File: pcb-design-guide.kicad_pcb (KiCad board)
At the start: 2 copper layers, 24 parts, among them SW1 SW_Push, U1 ATmega32U4-AU, Y1 16MHz

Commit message: PCB design complete
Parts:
- moved C2 24.5 mm to (192.3, 82.0), turned to 0 degrees
- moved C6 23.9 mm to (183.3, 59.6), turned to 90 degrees
- moved C3 13.3 mm to (182.8, 82.2)
- moved C7 12.8 mm to (175.9, 70.4), turned to 180 degrees
- moved C1 8.74 mm to (197.1, 67.2)
- moved C5 8.64 mm to (191.9, 59.4)
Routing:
- net COL1: track 0.00 -> 72.6 mm, vias 0 -> 1
- net +5V: track 41.7 -> 103.2 mm, vias 0 -> 6
- net COL0: track 0.00 -> 40.3 mm, vias 0 -> 1
- net Net-(R3-Pad2): track 14.2 -> 47.7 mm, vias 0 -> 2
- net Net-(C5-Pad1): track 24.5 -> 9.07 mm
- net GND: track 146.5 -> 153.7 mm
- net Net-(C7-Pad1): track 0.00 -> 5.24 mm
- net Net-(C6-Pad1): track 9.43 -> 11.0 mm

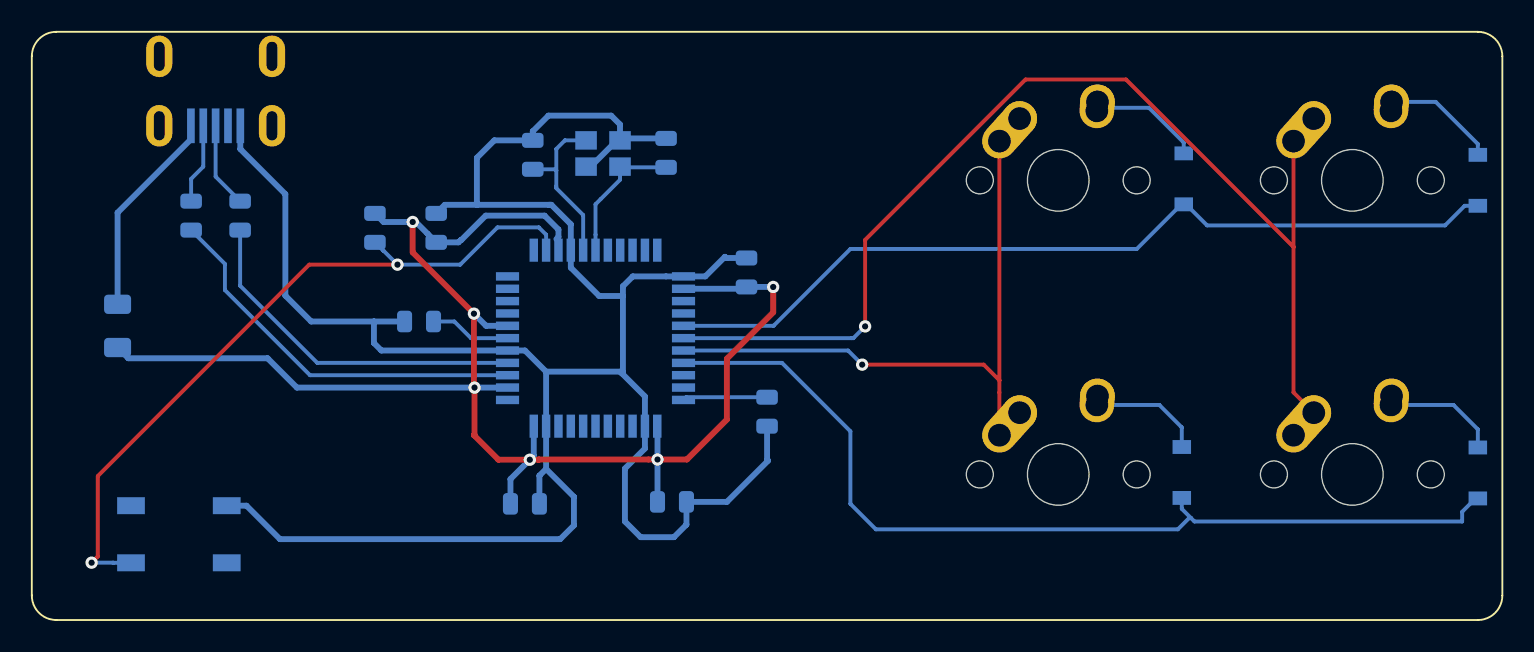
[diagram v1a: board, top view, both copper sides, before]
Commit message: Added ground fills
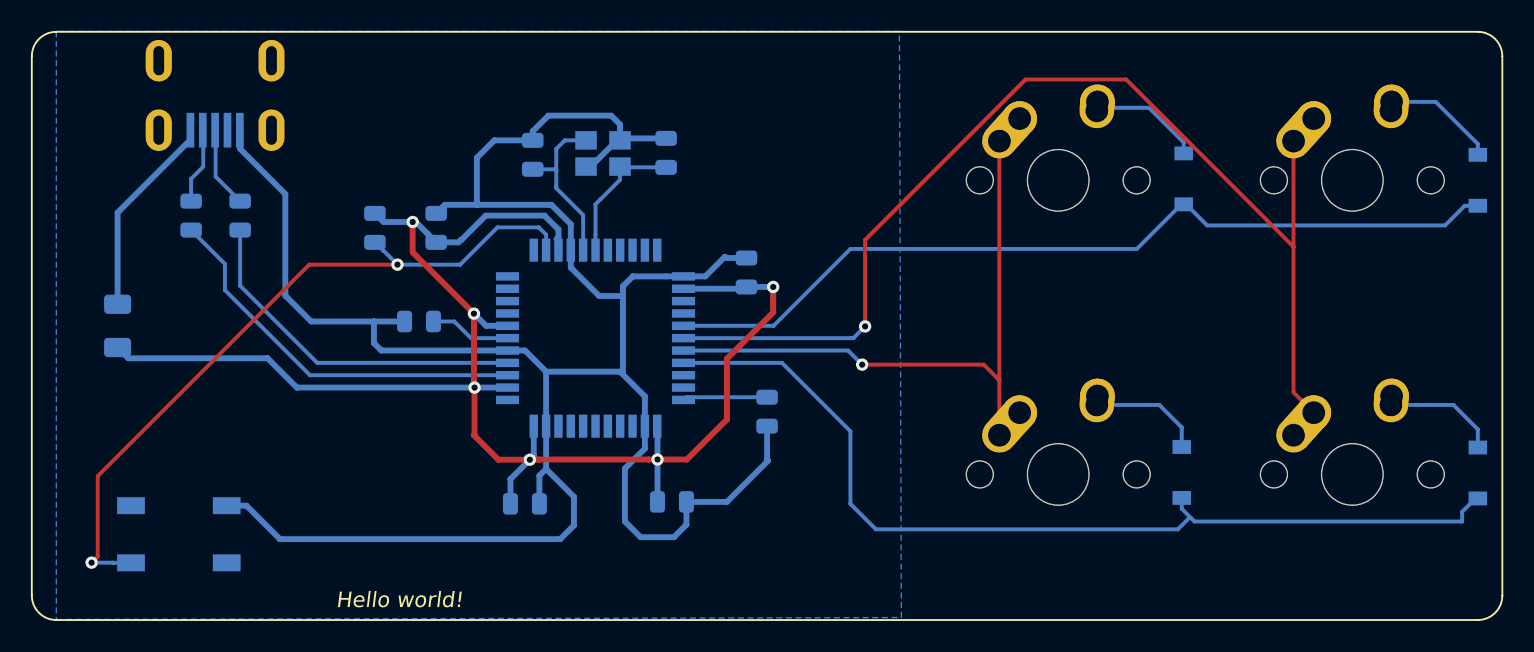
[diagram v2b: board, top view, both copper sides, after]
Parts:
- moved USB1 0.29 mm to (162.7, 53.5)
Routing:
- added copper zone on B.Cu, net GND
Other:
- board text added: "Hello world!"
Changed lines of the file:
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@@
   (general
     (thickness 1.6)
-    (drawings 8)
+    (drawings 9)
     (tracks 240)
     (zones 0)
@@
   )
   (module random-keyboard-parts:Molex-0548190589 (layer B.Cu)
-    (at 162.71875 53.18125 270)
+    (at 162.687 53.467 270)
     (attr smd)
     (fp_text reference USB1 (at 2.032 0 180) (layer B.SilkS)
@@
       (rotate (xyz 0 0 0))
     )
+  )
+  (gr_text "Hello world!" (at 174.625 88.392) (layer F.SilkS)
+    (effects (font (size 1 1) (thickness 0.15) italic))
   )
   (gr_line (start 152.4 51.59375) (end 244.475 51.59375) (layer F.SilkS) (width 0.12))
@@
   (segment (start 193.2 75.2625) (end 193.025 75.4375) (width 0.254) (layer B.Cu) (net 20))
   (segment (start 198.4375 75.2625) (end 193.2 75.2625) (width 0.254) (layer B.Cu) (net 20))
+  (zone (net 1) (net_name GND) (layer B.Cu) (hatch edge 0.508)
+    (connect_pads (clearance 0.508))
+    (min_thickness 0.254)
+    (fill yes (arc_segments 32) (thermal_gap 0.508) (thermal_bridge_width 0.508))
+    (polygon
+      (pts
+        (xy 152.4 51.562) (xy 152.4 89.662) (xy 207.137 89.535) (xy 207.01 51.562)
+      )
+    )
+  )
 )
